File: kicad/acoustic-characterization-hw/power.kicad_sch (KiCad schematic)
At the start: 14 parts, among them IC1 ECP5-BGA256, J2 Conn_01x04_Socket

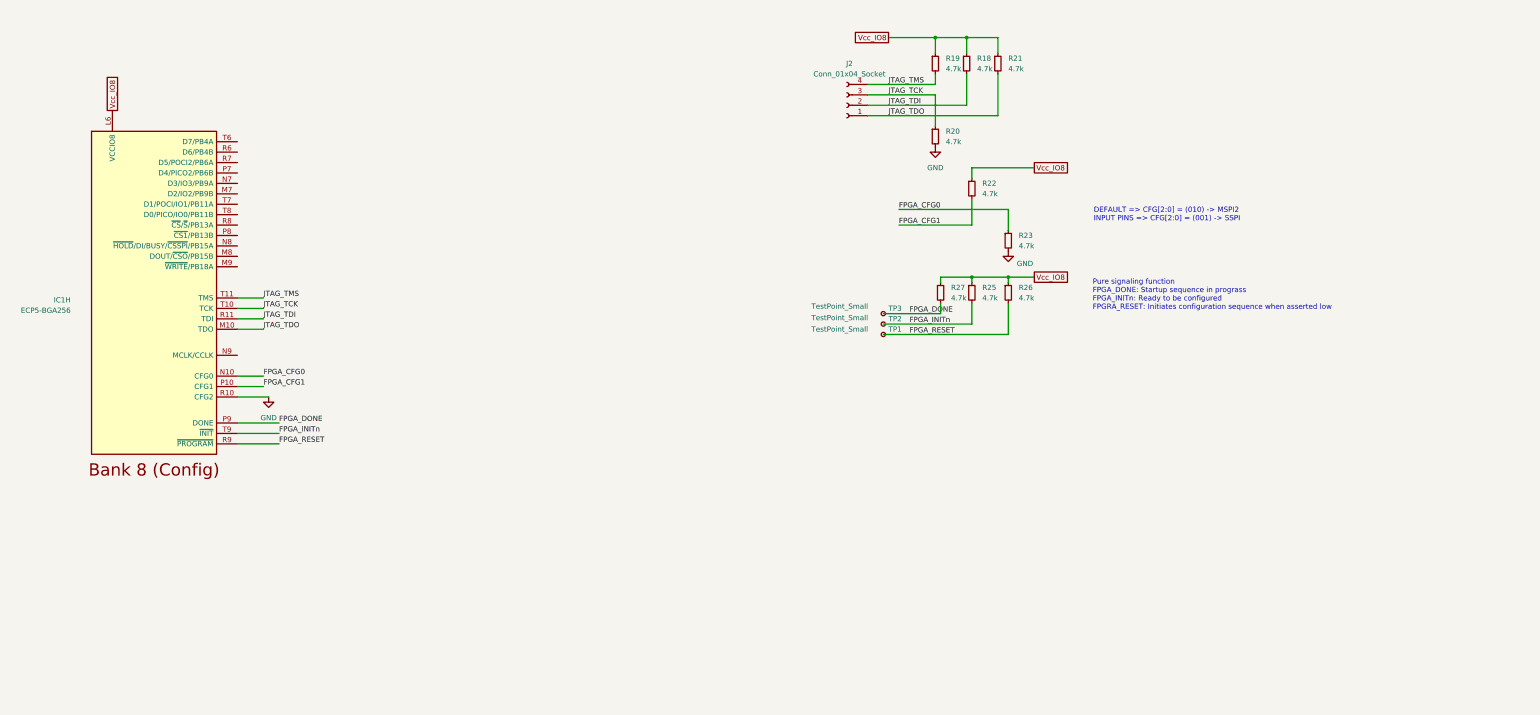
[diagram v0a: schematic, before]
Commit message: [kicad] Added initial config and jtag circuitrtry, added kicad symbol, added pinout + script for functionality checking (next) add qspi flash for boot
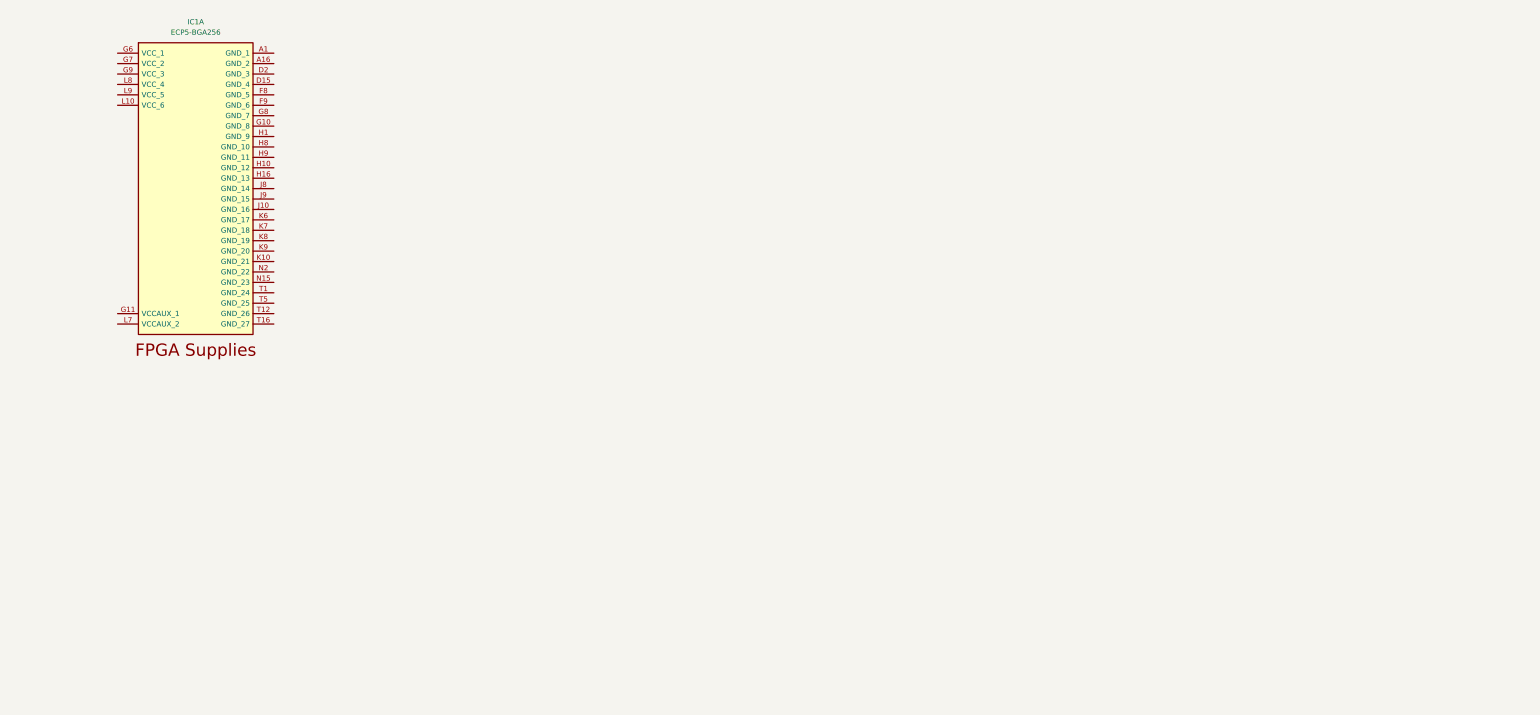
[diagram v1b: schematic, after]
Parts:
- removed IC1: ECP5-BGA256, BGA256C80P16X16_1400X1400X170, symbol ecp5bga256:ECP5-BGA256
- removed J2: Conn_01x04_Socket, symbol Connector:Conn_01x04_Socket
- removed R18, R19, R20, R21, R22, R23, R25, R26, R27: 4.7k, Resistor_SMD:R_0402_1005Metric, symbol Device:R_Small
- removed TP1, TP2, TP3: TestPoint_Small, symbol Connector:TestPoint_Small
- added IC1: ECP5-BGA256, BGA256C80P16X16_1400X1400X170, symbol ecp5bga256:ECP5-BGA256
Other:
- note removed: "DEFAULT => CFG[2:0] = (010) -> MSPI2 INPUT PINS => CFG[2:0] = (001) -> SSPI"
- note removed: "Pure signaling function FPGA_DONE: Startup sequence in prograss FPGA_INITn: Ready to be configured FPGRA_RESET: Initiates configuration sequence when asserted low"

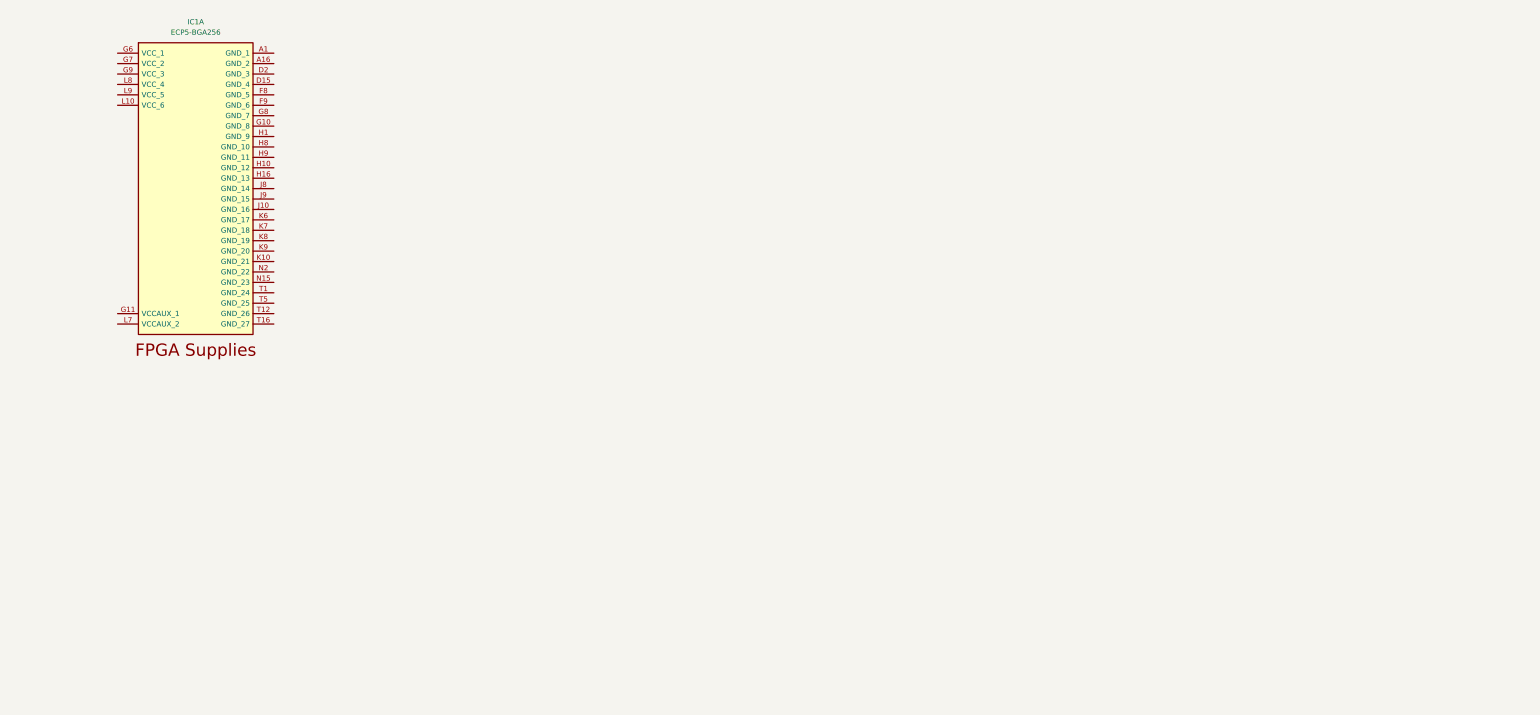
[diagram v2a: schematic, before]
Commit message: [kicad] Added switching regulators for 3.3, 1.25 and 2.5
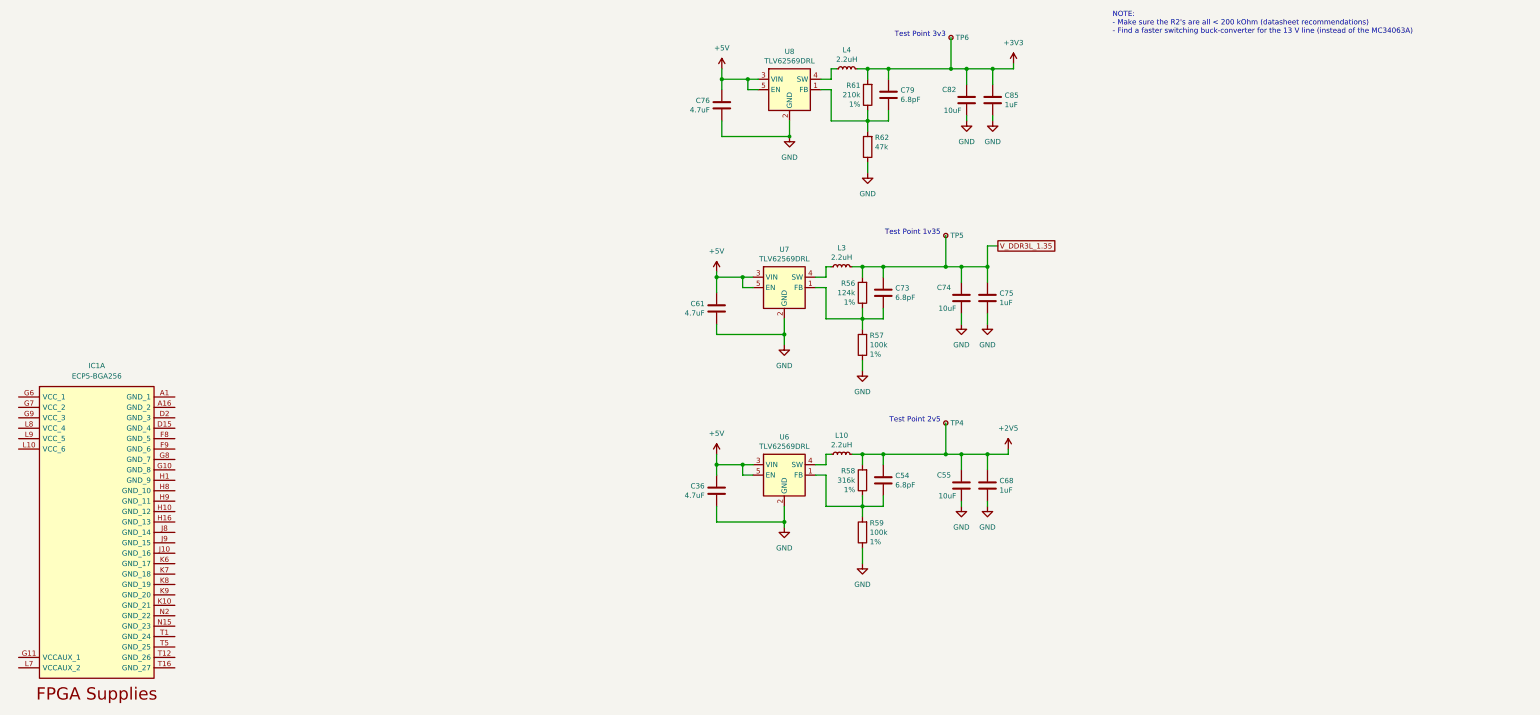
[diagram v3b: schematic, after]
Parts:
- added C36, C61, C76: 4.7uF, Capacitor_SMD:C_0402_1005Metric, symbol Device:C
- added C54, C73, C79: 6.8pF, Capacitor_SMD:C_0402_1005Metric, symbol Device:C
- added C55, C74, C82: 10uF, Capacitor_SMD:C_0603_1608Metric, symbol Device:C
- added C68, C75, C85: 1uF, Capacitor_SMD:C_0402_1005Metric, symbol Device:C
- added L10, L3, L4: 2.2uH, Inductor_SMD:L_0805_2012Metric, symbol Device:L_Small
- added R56: 124k, Resistor_SMD:R_0402_1005Metric, symbol Device:R
- added R57, R59: 100k, Resistor_SMD:R_0402_1005Metric, symbol Device:R
- added R58: 316k, Resistor_SMD:R_0402_1005Metric, symbol Device:R
- added R61: 210k, Resistor_SMD:R_0402_1005Metric, symbol Device:R
- added R62: 47k, Resistor_SMD:R_0402_1005Metric, symbol Device:R
- added TP4, TP5, TP6: TestPoint_Small, TestPoint:TestPoint_Pad_D1.5mm, symbol Connector:TestPoint_Small
- added U6, U7, U8: TLV62569DRL, Package_TO_SOT_SMD:SOT-563, symbol Regulator_Switching:TLV62569DRL
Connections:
- new net: L3.1, U7.4 (SW)
- new net: L4.1, U8.4 (SW)
- new net: C73.2, R56.1, R57.2, U7.1 (FB)
- new net: C54.2, R58.1, R59.2, U6.1 (FB)
- new net: C79.2, R61.1, R62.2, U8.1 (FB)
- new net: L10.1, U6.4 (SW)
- new net +2V5: C54.1, C55.1, C68.1, L10.2, R58.2, TP4.1
- new net +3V3: C79.1, C82.1, C85.1, L4.2, R61.2, TP6.1
- new net +5V: C36.1, C61.1, C76.1, U6.3 (VIN), U6.5 (EN), U7.3 (VIN), U7.5 (EN), U8.3 (VIN), U8.5 (EN)
- new net GND: C36.2, C55.2, C61.2, C68.2, C74.2, C75.2, C76.2, C82.2, C85.2, R57.1, R59.1, R62.1, U6.2 (GND), U7.2 (GND), U8.2 (GND)
- new net V_DDR3L_1.35: C73.1, C74.1, C75.1, L3.2, R56.2, TP5.1
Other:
- note added: "NOTE: - Make sure the R2's are all < 200 kOhm (datasheet recommendations) - Find a faster switching buck-converter for the 13 V line (instead of the MC34063A)"
- note added: "Test Point 1v35"
- note added: "Test Point 2v5"
- note added: "Test Point 3v3"
- moved on the sheet: IC1A
